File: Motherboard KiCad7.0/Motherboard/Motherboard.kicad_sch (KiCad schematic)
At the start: 83 parts, among them J1 USB_B_Micro, J10 SWD_01x04_Pin, J11 430450200, J12 430450200, J13 430450200, J14 430450200, J15 430450200, J2 B04B-XASK-1, J3 430450200, J4 430450200, Q10 AO3400A, Q11 AO3400A, Q12 AO3400A, Q13 AO3400A, Q7 AO3400A, Q8 AO4447A, Q9 AO3400A, SW1 SW_STM_RESET, SW3 SW_STM_BOOT_MODE, U1 STM32F103CBT6, U2 AMS1117-3.3, U3 LM66100DCKR, U4 LM66100DCKR, U5 LM66100DCKR, U6 Micro_SD_Reader, Y1 X322516MMB4SI

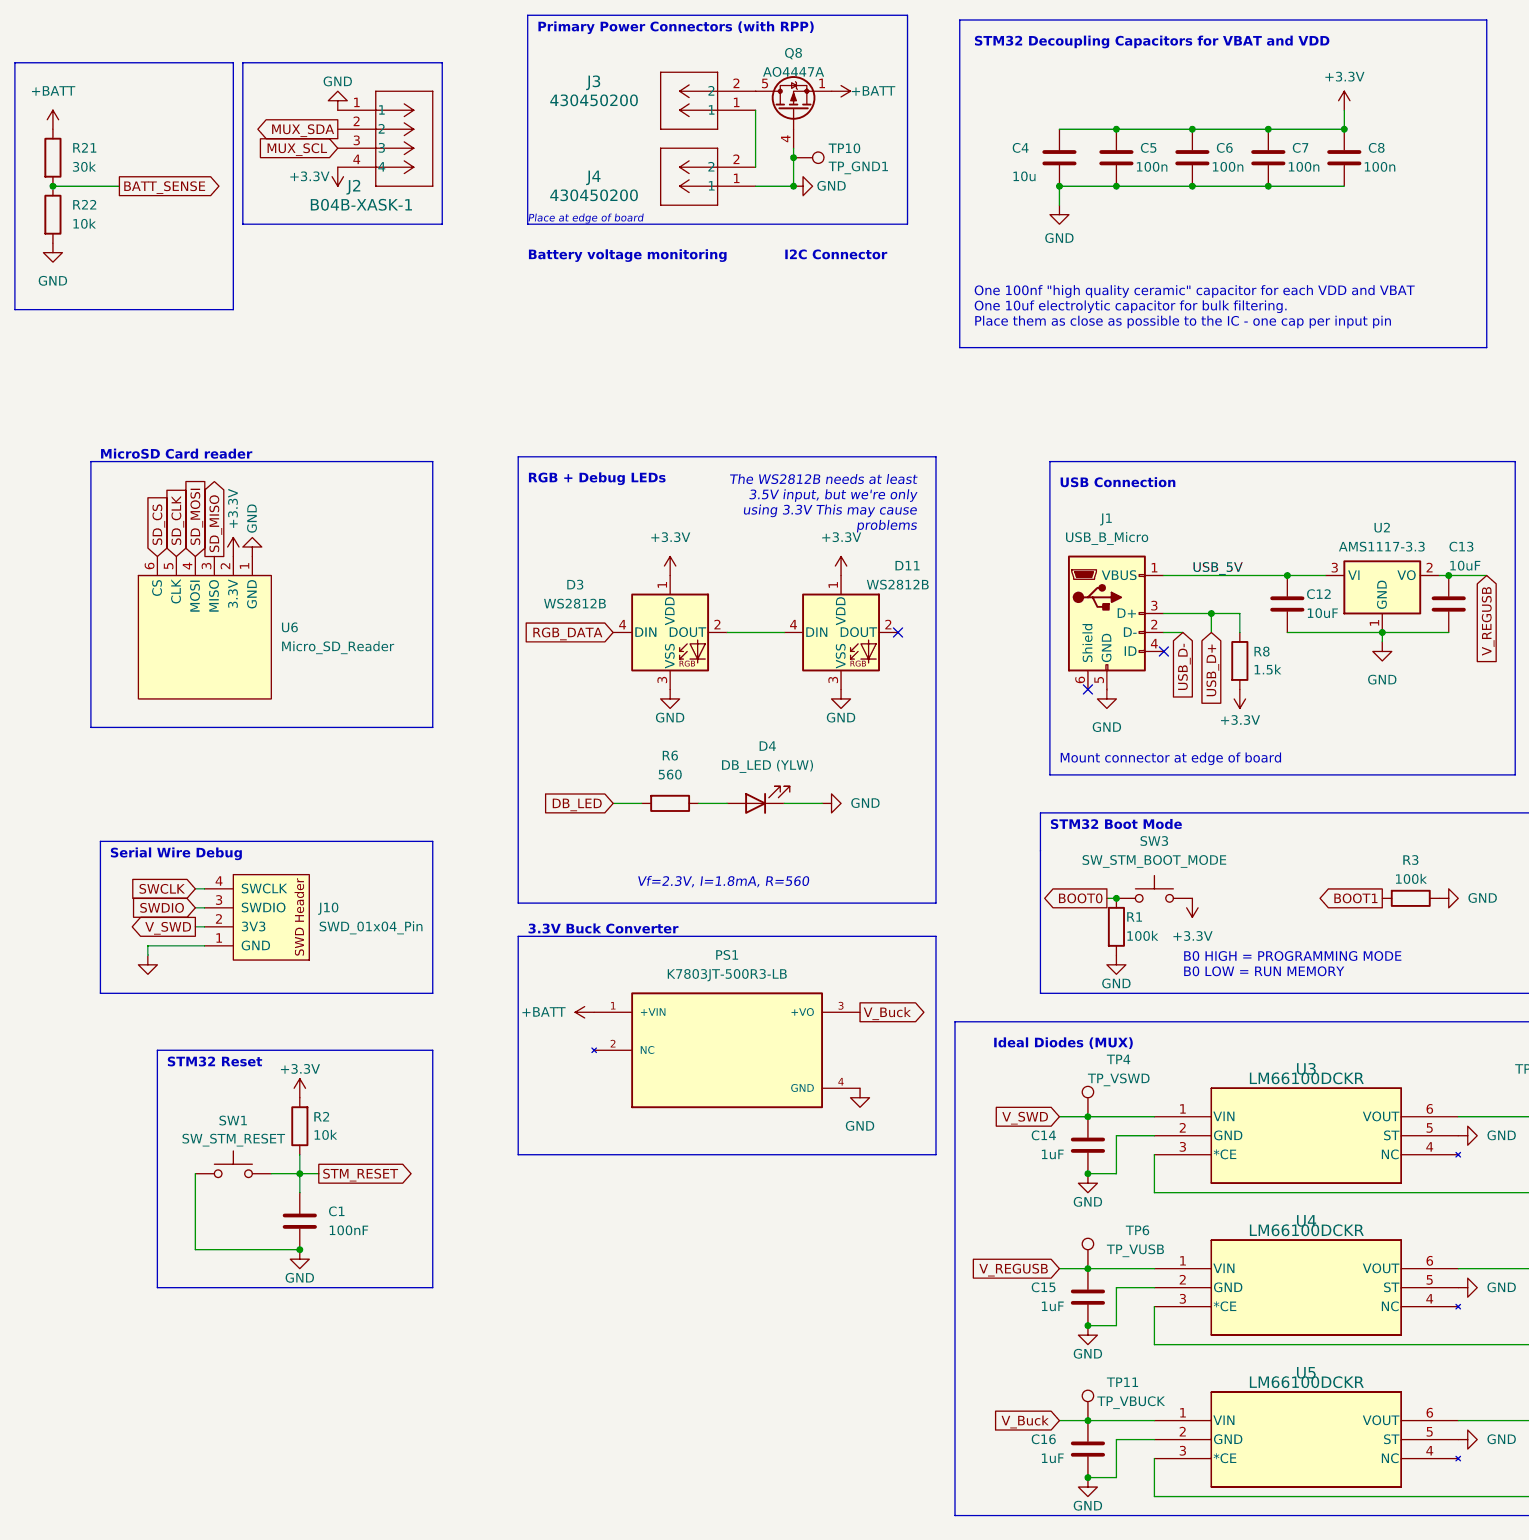
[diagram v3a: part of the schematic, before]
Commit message: Fixed footprint library issues
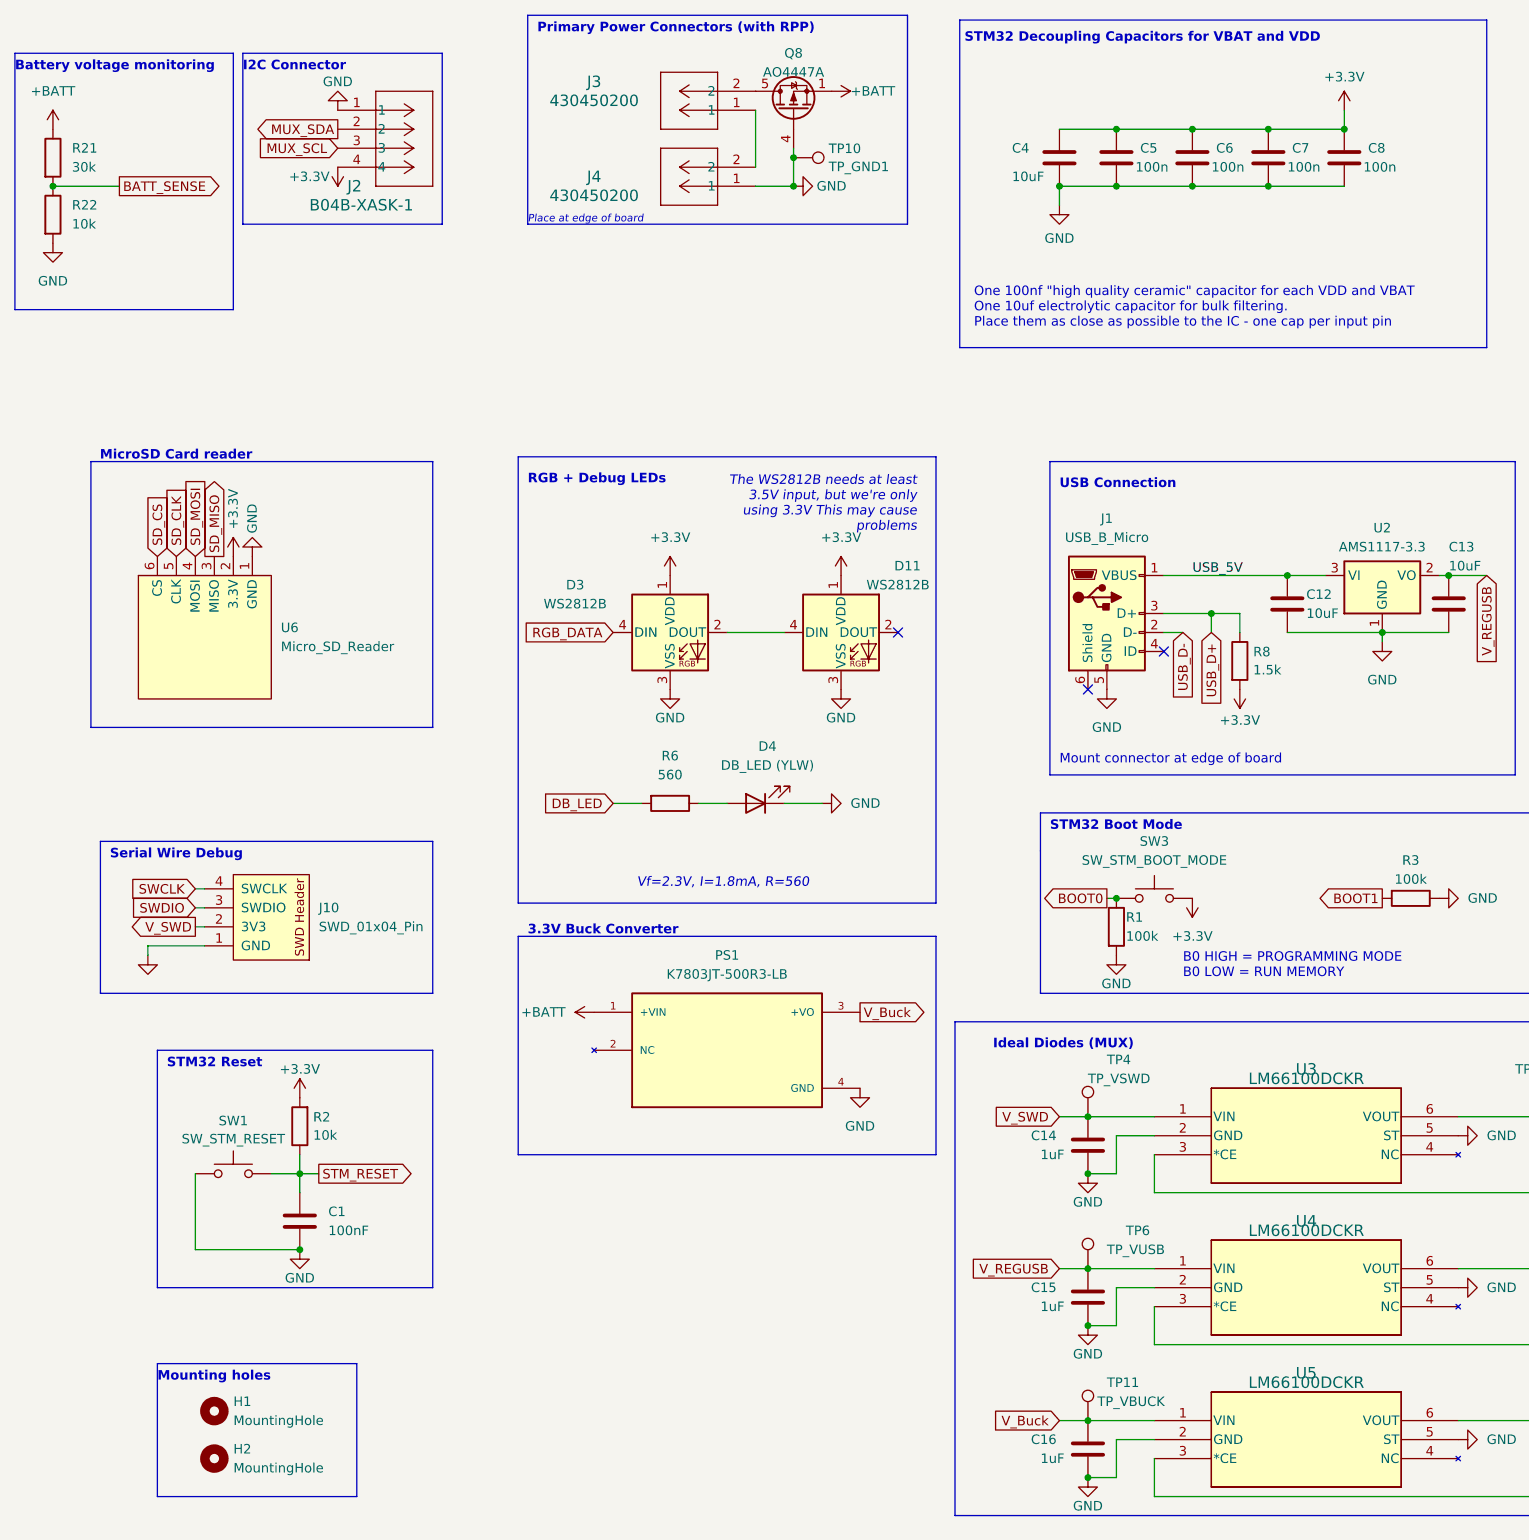
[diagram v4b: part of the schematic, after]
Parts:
- added H1, H2: MountingHole, symbol Mechanical:MountingHole
- C4: value 10u -> 10uF
- J1: footprint footprints:USB_Micro-B_Amphenol_10118194_Horizontal -> USB_Micro-B_Amphenol_10118194_Horizontal:USB_Micro-B_Amphenol_10118194_Horizontal
- J11, J12, J13, J14, J15, J4: footprint CON_430450200_MOL -> CONN 0430450200:CON_430450200_MOL
- R21, R22: footprint (none) -> Resistor_SMD:R_0603_1608Metric
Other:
- note added: "Mounting holes"
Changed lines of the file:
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@@
     (stroke (width 0) (type default))
   )
-  (rectangle (start 20.32 40.64) (end 49.53 73.66)
+  (rectangle (start 20.32 39.37) (end 49.53 73.66)
     (stroke (width 0) (type default))
     (fill (type none))
@@
     (fill (type none))
   )
+  (rectangle (start 39.37 214.63) (end 66.04 232.41)
+    (stroke (width 0) (type default))
+    (fill (type none))
+  )
   (rectangle (start 146.685 34.925) (end 217.17 78.74)
     (stroke (width 0) (type default))
@@
     (fill (type none))
   )
-  (rectangle (start 50.8 40.64) (end 77.47 62.23)
+  (rectangle (start 50.8 39.37) (end 77.47 62.23)
     (stroke (width 0) (type solid))
     (fill (type none))
@@
     (fill (type none))
   )
+  (text "Mounting holes" (at 39.37 217.17 0)
+    (effects (font (size 1.27 1.27) (thickness 0.254) bold) (justify left bottom))
+  )
   (text "USB Connection" (at 160.02 97.79 0)
     (effects (font (size 1.27 1.27) (thickness 0.254) bold) (justify left bottom))
   )
-  (text "STM32 Decoupling Capacitors for VBAT and VDD" (at 148.59 38.735 0)
+  (text "STM32 Decoupling Capacitors for VBAT and VDD" (at 147.32 38.1 0)
     (effects (font (size 1.27 1.27) (thickness 0.254) bold) (justify left bottom))
   )
-  (text "I2C Connector" (at 123.19 67.31 0)
+  (text "I2C Connector" (at 50.8 41.91 0)
     (effects (font (size 1.27 1.27) (thickness 0.254) bold) (justify left bottom))
   )
@@
     (effects (font (size 1.27 1.27) (thickness 0.254) bold) (justify left bottom))
   )
-  (text "Battery voltage monitoring\n" (at 88.9 67.31 0)
+  (text "Battery voltage monitoring\n" (at 20.32 41.91 0)
     (effects (font (size 1.27 1.27) (thickness 0.254) bold) (justify left bottom))
   )
@@
     )
   )
+  (symbol (lib_id "Mechanical:MountingHole") (at 46.99 227.33 0) (unit 1)
+    (in_bom yes) (on_board yes) (dnp no) (fields_autoplaced)
+    (property "Reference" "H2" (at 49.53 226.06 0)
+      (effects (font (size 1.27 1.27)) (justify left))
+    )
+    (property "Value" "MountingHole" (at 49.53 228.6 0)
+      (effects (font (size 1.27 1.27)) (justify left))
+    )
+    (property "Footprint" "" (at 46.99 227.33 0)
+      (effects (font (size 1.27 1.27)) hide)
+    )
+    (property "Datasheet" "~" (at 46.99 227.33 0)
+      (effects (font (size 1.27 1.27)) hide)
+    )
+    (instances
+      (project "Motherboard"
+        (path "/6c6aab7b-9fc7-4161-8073-41667e18c629"
+          (reference "H2") (unit 1)
+        )
+      )
+    )
+  )
   (symbol (lib_id "power:GND") (at 213.36 224.79 90) (unit 1)
     (in_bom yes) (on_board yes) (dnp no) (fields_autoplaced)
@@
       (effects (font (size 1.524 1.524)))
     )
-    (property "Footprint" "CON_430450200_MOL" (at 353.06 64.77 0)
+    (property "Footprint" "CONN 0430450200:CON_430450200_MOL" (at 353.06 64.77 0)
       (effects (font (size 1.27 1.27) italic) hide)
     )
@@
       (effects (font (size 1.524 1.524)))
     )
-    (property "Footprint" "CON_430450200_MOL" (at 353.06 36.83 0)
+    (property "Footprint" "CONN 0430450200:CON_430450200_MOL" (at 353.06 36.83 0)
       (effects (font (size 1.27 1.27) italic) hide)
     )
@@
       (effects (font (size 1.27 1.27)) (justify left))
     )
-    (property "Value" "10u" (at 153.67 55.88 0)
+    (property "Value" "10uF" (at 153.67 55.88 0)
       (effects (font (size 1.27 1.27)) (justify left))
     )
@@
       (effects (font (size 1.27 1.27)) (justify left))
     )
-    (property "Footprint" "" (at 23.622 60.96 90)
+    (property "Footprint" "Resistor_SMD:R_0603_1608Metric" (at 23.622 60.96 90)
       (effects (font (size 1.27 1.27)) hide)
     )
@@
       (effects (font (size 1.524 1.524)))
     )
-    (property "Footprint" "CON_430450200_MOL" (at 353.06 149.86 0)
+    (property "Footprint" "CONN 0430450200:CON_430450200_MOL" (at 353.06 149.86 0)
       (effects (font (size 1.27 1.27) italic) hide)
     )
@@
       (effects (font (size 1.524 1.524)))
     )
-    (property "Footprint" "CON_430450200_MOL" (at 353.06 120.65 0)
+    (property "Footprint" "CONN 0430450200:CON_430450200_MOL" (at 353.06 120.65 0)
       (effects (font (size 1.27 1.27) italic) hide)
     )
@@
       (effects (font (size 1.524 1.524)))
     )
-    (property "Footprint" "CON_430450200_MOL" (at 353.06 92.71 0)
+    (property "Footprint" "CONN 0430450200:CON_430450200_MOL" (at 353.06 92.71 0)
       (effects (font (size 1.27 1.27) italic) hide)
     )
@@
     )
   )
+  (symbol (lib_id "Mechanical:MountingHole") (at 46.99 220.98 0) (unit 1)
+    (in_bom yes) (on_board yes) (dnp no) (fields_autoplaced)
+    (property "Reference" "H1" (at 49.53 219.71 0)
+      (effects (font (size 1.27 1.27)) (justify left))
+    )
+    (property "Value" "MountingHole" (at 49.53 222.25 0)
+      (effects (font (size 1.27 1.27)) (justify left))
+    )
+    (property "Footprint" "" (at 46.99 220.98 0)
+      (effects (font (size 1.27 1.27)) hide)
+    )
+    (property "Datasheet" "~" (at 46.99 220.98 0)
+      (effects (font (size 1.27 1.27)) hide)
+    )
+    (instances
+      (project "Motherboard"
+        (path "/6c6aab7b-9fc7-4161-8073-41667e18c629"
+          (reference "H1") (unit 1)
+        )
+      )
+    )
+  )
   (symbol (lib_id "power:GND") (at 361.95 173.99 90) (unit 1)
     (in_bom yes) (on_board yes) (dnp no) (fields_autoplaced)
@@
       (effects (font (size 1.27 1.27)) (justify left))
     )
-    (property "Footprint" "" (at 23.622 53.34 90)
+    (property "Footprint" "Resistor_SMD:R_0603_1608Metric" (at 23.622 53.34 90)
       (effects (font (size 1.27 1.27)) hide)
     )
@@
       (effects (font (size 1.524 1.524)))
     )
-    (property "Footprint" "CON_430450200_MOL" (at 123.19 60.96 0)
+    (property "Footprint" "CONN 0430450200:CON_430450200_MOL" (at 123.19 60.96 0)
       (effects (font (size 1.27 1.27) italic) hide)
     )
@@
       (effects (font (size 1.27 1.27)))
     )
-    (property "Footprint" "footprints:USB_Micro-B_Amphenol_10118194_Horizontal" (at 170.18 115.57 0)
+    (property "Footprint" "USB_Micro-B_Amphenol_10118194_Horizontal:USB_Micro-B_Amphenol_10118194_Horizontal" (at 170.18 115.57 0)
       (effects (font (size 1.27 1.27)) hide)
     )

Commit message: Started PCB layout
Routed all 3.3V, and +BATT traces and started routing signal traces
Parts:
- H1, H2: footprint (none) -> Rod_Mounting_Hole_6.7564mm:Rod_Mounting_Hole_6.7564mm
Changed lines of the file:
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@@
       (effects (font (size 1.27 1.27)) (justify left))
     )
-    (property "Footprint" "" (at 46.99 227.33 0)
+    (property "Footprint" "Rod_Mounting_Hole_6.7564mm:Rod_Mounting_Hole_6.7564mm" (at 46.99 227.33 0)
       (effects (font (size 1.27 1.27)) hide)
     )
@@
       (effects (font (size 1.27 1.27)) (justify left))
     )
-    (property "Footprint" "" (at 46.99 220.98 0)
-      (effects (font (size 1.27 1.27)) hide)
-    )
+    (property "Footprint" "Rod_Mounting_Hole_6.7564mm:Rod_Mounting_Hole_6.7564mm" (at 46.99 220.98 0)
+      (effects (font (size 1.27 1.27)) hide)
+    )

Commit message: motherboard pcb layout - Mohamad
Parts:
- removed BZ1: PKM13EPYH4000, Buzzer_12.6x9.5RM5.0:Buzzer_12.6x9.5RM5.0, symbol Device:Buzzer
- removed D10, D12, D13, D14, D15, D16, D17: 1N5819WS, Diode_SMD:D_SOD-323, symbol Diode:1N5819WS
- removed H1, H2: MountingHole, Rod_Mounting_Hole_6.7564mm:Rod_Mounting_Hole_6.7564mm, symbol Mechanical:MountingHole
- removed J10: SWD_01x04_Pin, SWD_Header:SWD_PinHeader_1x04_P2.54mm_Horizontal, symbol EdgeConnector:SWD_01x04_Pin
- removed J11, J12, J13, J14, J15, J3, J4: 430450200, CONN 0430450200:CON_430450200_MOL, symbol CONN 0430450200:430450200
- removed J2: B04B-XASK-1, B04B_XASK_1:CONN_B04B-XASK-1_JST, symbol B04B_XASK_1:B04B-XASK-1
- removed PS1: K7803JT-500R3-LB, CONV_K7812JT-500R3-LB:CONV_K7812JT-500R3-LB, symbol K7812JT-500R3-LB:K7812JT-500R3-LB
- removed Q10, Q11, Q12, Q13, Q7, Q9: AO3400A, Package_TO_SOT_SMD:SOT-23, symbol Transistor_FET:AO3400A
- removed Q8: AO4447A, Package_SO:SOIC-8_3.9x4.9mm_P1.27mm, symbol Transistor_FET:IRF7404
- removed R21: 30k, Resistor_SMD:R_0603_1608Metric, symbol Device:R
- removed R22, R23, R24, R25, R26, R27: 10k, Resistor_SMD:R_0603_1608Metric, symbol Device:R
- removed R28, R29, R30, R31, R32: 510R, Resistor_SMD:R_0603_1608Metric, symbol Device:R
- removed R33: 1k, Resistor_SMD:R_0603_1608Metric, symbol Device:R
- removed SW3: SW_STM_BOOT_MODE, Button_Switch_SMD:SW_Push_1P1T_XKB_TS-1187A, symbol Switch:SW_MEC_5G
- removed TP11: TP_VBUCK, TestPoint:TestPoint_Pad_1.5x1.5mm, symbol Connector:TestPoint
- removed U3, U4, U5: LM66100DCKR, LMR66100:SC-70-6_Handsoldering, symbol QRET_Buck_PSU-symbols:LM66100DCKR
- removed U6: Micro_SD_Reader, MicroSD Card Reader:MicroSD Card Reader, symbol MicroSD Card Reader:Micro_SD_Reader
- added C17: 4.7uF, Capacitor_SMD:C_0805_2012Metric, symbol Device:C
- added C18, C19: 100nF, Capacitor_SMD:C_0603_1608Metric, symbol Device:C
- added C20, C21: 22uF, Capacitor_SMD:C_0805_2012Metric, symbol Device:C
- added C22: 100uF, Capacitor_SMD:CP_Elec_6.3x5.9, symbol Device:C_Polarized
- added J2: SWD_01x04_Pin, SWD_Header:SWD_PinHeader_1x04_P2.54mm_Horizontal, symbol QRET_Edge_Connector:SWD_01x04_Pin
- added J? (x2): 430450200, CONN 0430450200:CON_430450200_MOL, symbol CONN 0430450200:430450200
- added L1: 5.6uH, Inductor_SMD:L_Bourns_SRN8040TA, symbol Device:L
- added Q7: AO4447A, Package_SO:SOIC-8_3.9x4.9mm_P1.27mm, symbol Transistor_FET:IRF7404
- added SW2: SW_STM_BOOT_MODE, PTS636:PTS636_SK43_SMTR_LFS, symbol Switch:SW_Push
- added TP7: TP_MUX, TestPoint:TestPoint_Pad_1.5x1.5mm, symbol Connector:TestPoint
- added TP8: TP_BATT1, TestPoint:TestPoint_Pad_2.0x2.0mm, symbol Connector:TestPoint
- added TP9: TP_3.3V_A, TestPoint:TestPoint_Pad_2.0x2.0mm, symbol Connector:TestPoint
- added U3, U4, U5: LM66100DCKR, LMR66100:SC-70-6, symbol QRET_Buck_PSU:LM66100DCKR
- added U6: LMR51430XDDCR, Package_TO_SOT_SMD:SOT-23-6_Handsoldering, symbol QRET_Buck_PSU-symbols:LMR51430XDDCR
- added U?: DEV-13743, DEV-13743:MODULE_DEV-13743, symbol DEV-13743:DEV-13743
- C10, C11: footprint Capacitor_SMD:C_0805_2012Metric -> Capacitor_SMD:CP_Elec_4x5.4
- C4: value 10uF -> 10u
- J1: footprint USB_Micro-B_Amphenol_10118194_Horizontal:USB_Micro-B_Amphenol_10118194_Horizontal -> footprints:USB_Micro-B_Amphenol_10118194_Horizontal
- R19: value 10k -> 100k; LCSC C25804 -> C25803
- R20: value 510R -> 22k; LCSC C23193 -> C31850
- R6: value 560 -> 560R
- SW1: footprint Button_Switch_SMD:SW_Push_1P1T_XKB_TS-1187A -> PTS636:PTS636_SK43_SMTR_LFS
- TP4: value TP_VSWD -> TP_VSTACK
- TP5: value TP_MUX -> TP_VUSB
- TP6: value TP_VUSB -> TP_VSWD
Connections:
- net SD_CS is gone; now on net Pump: U1.14 (PA4)
- net V_Buck is gone; now on net V_SWD: C16.1
- net +3.3V: now also SW2.2; no longer D11.1 (VDD), D3.1 (VDD), TP5.1
- net BOOT0: now also R1.2, SW2.1; no longer R1.1
- net BUZZER: no longer R19.2, R20.2
- net GND: now also R1.1, R20.2, C17.2, C18.2, C20.2, C21.2, C22.2, J2.1 (GND), J?.1, Q7.4 (G), U3.2 (GND), U3.5 (ST), U4.2 (GND), U4.5 (ST), U5.2 (GND), U5.5 (ST), U6.1 (GND), U?.1 (GND); no longer R1.2, R19.1
- net Pump: no longer U1.29 (PA8)
- net SWCLK: now also J2.4 (SWCLK)
- net SWDIO: now also J2.3 (SWDIO)
- net V_REGUSB: now also TP5.1, U4.1 (VIN); no longer TP6.1
- net V_SWD: now also TP6.1, J2.2 (3V3), U5.1 (VIN); no longer C14.1, TP4.1
- net at R20.1: now also R19.2, U6.4 (FB)
- net CURR_SENSE: now reaches U1.19 (PB1)
- net CS_FL: now reaches U1.25 (PB12)
- net SCK_FL: now reaches U1.26 (PB13)
- net MUX_SCL: no longer names the net of U1.21 (PB10)
- net MUX_SDA: no longer names the net of U1.22 (PB11)
- net SD_CLK: no longer names the net of U1.15 (PA5)
- net SD_MISO: no longer names the net of U1.16 (PA6)
- net SD_MOSI: no longer names the net of U1.17 (PA7)
- new net: C19.1, L1.1, U6.2 (SW)
- new net: C19.2, U6.6 (CB)
- new net: J?.1, J?.2
- new net: J?.2, Q7.5 (D), Q7.6 (D), Q7.7 (D), Q7.8 (D)
- new net 3.3V_A: C20.1, C21.1, C22.1, D11.1 (VDD), D3.1 (VDD), L1.2, R19.1, TP9.1
- new net BATT_A: C17.1, C18.1, Q7.1 (S), Q7.2 (S), Q7.3 (S), TP8.1, U6.3 (VIN), U6.5 (EN)
- new net V_MUX: TP7.1, U3.3 (*CE), U3.6 (VOUT), U4.3 (*CE), U4.6 (VOUT), U5.3 (*CE), U5.6 (VOUT)
- new net V_PSU: C14.1, TP4.1, U3.1 (VIN)
- no-connect marks 15 -> 18
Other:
- added sheet Motherboard P2 (Motherboard P2.kicad_sch)
- note added: "FOLLOW LAYOUT EXAMPLE (9.4.2) FROM DATASHEET LMR51430: PFM @ 500kHz (simpler routing & higher efficiency)"
- note added: "Max Output: 2.5A"
- note added: "Primary 3.3V Buck Regulator"
- note added: "Rfbt=100k, Rfbb=22k Vout = ((Rfbt*0.6)/Rfbb)+0.6 Vout = 3.327V"
- note removed: "3.3V Buck Converter"
- note removed: "Air Pump"
- note removed: "Battery voltage monitoring"
- note removed: "Buzzer"
- note removed: "I2C Connector"
- note removed: "MicroSD Card reader"
- note removed: "Mounting holes"
- note removed: "Solenoid Valves"
- company: Queen's Rocket Engineering Team -> (none)
- moved on the sheet: C1, C10, C11, C12, C13, C2, C3, C4, C5, C6, C7, C8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
